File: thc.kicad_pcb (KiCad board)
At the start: 2 copper layers, 132 x 100 mm, 53 parts, among them CON1 BARREL_JACK, IC1 4N25, J1 DB9, J2 DB25, U1 LM358N, U2 ARDUINO_MINI_PRO, U3 CNY74-4, U4 7805, U5 ISOL_PWR, U6 LM324N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

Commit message: Finalized design, produced PCB, started testing it
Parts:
- added Q1: BC547, TO92, F.Cu at (73.9, 39.8)
- added R22: 10K, R3-LARGE_PADS, F.Cu at (70.7, 49.0)
- added R23: 1K, R3-LARGE_PADS, F.Cu at (78.0, 33.5)
- R21: value 100R -> 1K
- U6: value LM324N -> 74HC04
- moved R15 9.25 mm to (136.5, 66.7), turned to 180 degrees
- moved D4 8.25 mm to (78.0, 44.2)
- moved R13 7.96 mm to (143.5, 43.8)
- moved C2 7.74 mm to (134.6, 46.2)
- moved J2 6.41 mm to (140.2, 95.8)
- moved R12 3.24 mm to (138.4, 43.8)
- moved U6 2.62 mm to (141.0, 54.6)
- moved R14 1.42 mm to (132.1, 62.9), turned to 180 degrees
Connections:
- D4 pad 2: N-0000010 -> N-000006
- J2 pad 18: (no net) -> GNDA
- J2 pad 19: (no net) -> GNDA
- J2 pad 20: (no net) -> GNDA
- J2 pad 21: (no net) -> GNDA
- J2 pad 22: (no net) -> GNDA
- J2 pad 23: (no net) -> GNDA
- J2 pad 24: (no net) -> GNDA
- J2 pad 25: (no net) -> GNDA
- R12 pad 1: N-0000039 -> N-0000048
- R13 pad 1: N-0000040 (its old number) -> N-0000049
- R14 pad 1: N-0000041 -> N-0000051
- R15 pad 1: N-0000038 (its old number) -> N-0000050
- R16 pad 1: I_THC_INP3 -> I_THC_INP4
- R17 pad 1: I_THC_INP4 -> I_THC_INP3
- R21 pad 2: N-0000010 -> N-0000023
- U2 pad 10: I_THC_INP3 -> I_THC_INP4
- U2 pad 6: N-0000010 -> N-000006
- U2 pad 9: I_THC_INP4 -> I_THC_INP3
- U6 pad 1: N-0000041 -> /Isolation/U_THC_INP4
- U6 pad 10: /Isolation/U_THC_INP2 -> N-0000049
- U6 pad 11: GNDA -> /Isolation/U_THC_INP2
- U6 pad 12: /Isolation/U_THC_INP1 -> N-0000048
- U6 pad 13: N-0000039 -> /Isolation/U_THC_INP1
- U6 pad 14: N-0000039 -> +5VA
- U6 pad 2: N-0000041 -> N-0000051
- U6 pad 4: +5VA -> N-0000050
- U6 pad 5: /Isolation/U_THC_INP4 -> (no net)
- U6 pad 6: N-0000038 (its old number) -> (no net)
- U6 pad 7: N-0000038 (its old number) -> GNDA
- U6 pad 8: N-0000040 (its old number) -> (no net)
- U6 pad 9: N-0000040 (its old number) -> (no net)
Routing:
- net GNDA: track 228.7 -> 320.3 mm
- net +5V: track 146.2 -> 200.5 mm, vias 2 -> 3
- net /Isolation/U_THC_INP3: track 61.7 -> 26.5 mm
- net N-0000010: track 32.9 -> 0.00 mm
- net N-000006: track 0.00 -> 28.4 mm
- net /Isolation/U_THC_INP4: track 56.0 -> 29.6 mm
- net /Isolation/U_THC_OUT1: track 128.6 -> 107.7 mm, vias 0 -> 2
- net +5VA: track 144.8 -> 126.3 mm
- net GND: track 423.1 -> 440.4 mm
- net N-0000046: track 31.0 -> 17.8 mm
- net /Isolation/U_THC_OUT5: track 81.5 -> 68.4 mm
- net /Isolation/U_THC_OUT4: track 79.6 -> 67.4 mm
- net N-0000023: track 0.00 -> 11.1 mm
- net I_THC_OUT4: track 66.6 -> 77.3 mm
- net /Isolation/U_THC_INP2: track 54.1 -> 44.8 mm
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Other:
- board size 132 x 100 mm -> 130 x 100 mm
- board text added: "RV2014"
- board text added: "THC"

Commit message: Done some more tests
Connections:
- U2 pad 21: (no net) -> /AMP_SIG

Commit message: Fixes completely wrong schematics and PCB layout
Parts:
- removed D10, D11, D12, D13: ZENER, D3
- moved R18 1.91 mm to (109.3, 50.8), turned to 180 degrees
- moved R17 1.22 mm to (109.4, 53.4), turned to 180 degrees
- moved R16 0.20 mm to (109.4, 61.0)
- turned R19 to 180 degrees
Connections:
- R16 pad 1: I_THC_INP4 -> GND
- R16 pad 2: N-0000063 -> I_THC_INP4
- R17 pad 2: N-0000066 (its old number) -> GND
- R18 pad 2: N-0000065 (its old number) -> GND
- R19 pad 2: N-0000064 -> GND
- U7 pad 10: GND -> +5V
- U7 pad 11: GND -> +5V
- U7 pad 12: N-0000065 (its old number) -> I_THC_INP2
- U7 pad 13: N-0000066 (its old number) -> I_THC_INP3
- U7 pad 14: GND -> +5V
- U7 pad 15: GND -> +5V
- U7 pad 16: N-0000063 -> I_THC_INP4
- U7 pad 9: N-0000064 -> I_THC_INP1
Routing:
- net +5V: track 200.5 -> 249.2 mm
- net I_THC_INP4: track 62.6 -> 84.1 mm
- net I_THC_INP2: track 55.1 -> 75.8 mm
- net GND: track 440.4 -> 420.6 mm, vias 0 -> 2
- net I_THC_INP1: track 51.5 -> 70.6 mm
- net I_THC_INP3: track 59.1 -> 77.7 mm
- net N-0000064: track 11.8 -> 0.00 mm
- net N-0000063: track 11.8 -> 0.00 mm
- net N-0000065 (its old number): track 6.50 -> 0.00 mm
- net N-0000066 (its old number): track 6.24 -> 0.00 mm

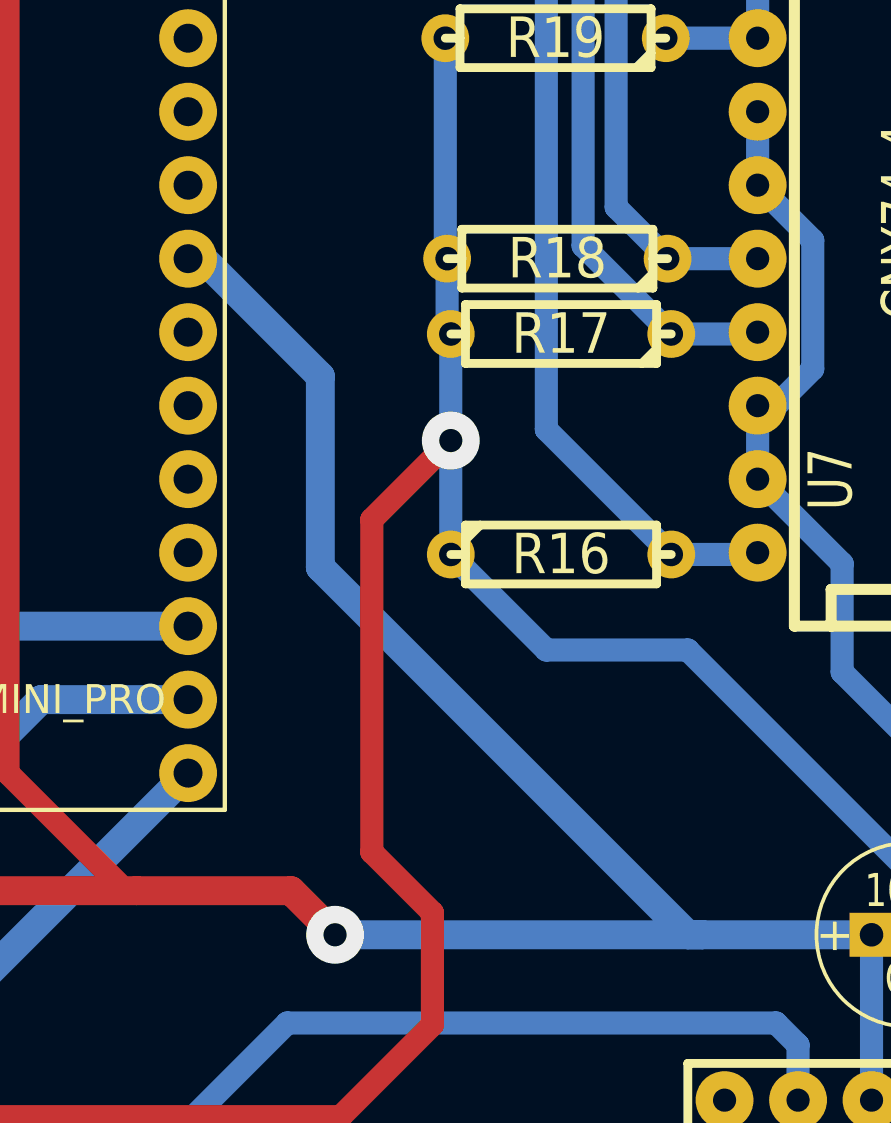
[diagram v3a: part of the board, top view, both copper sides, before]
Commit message: Fixed wrong power pin being used in Atmega
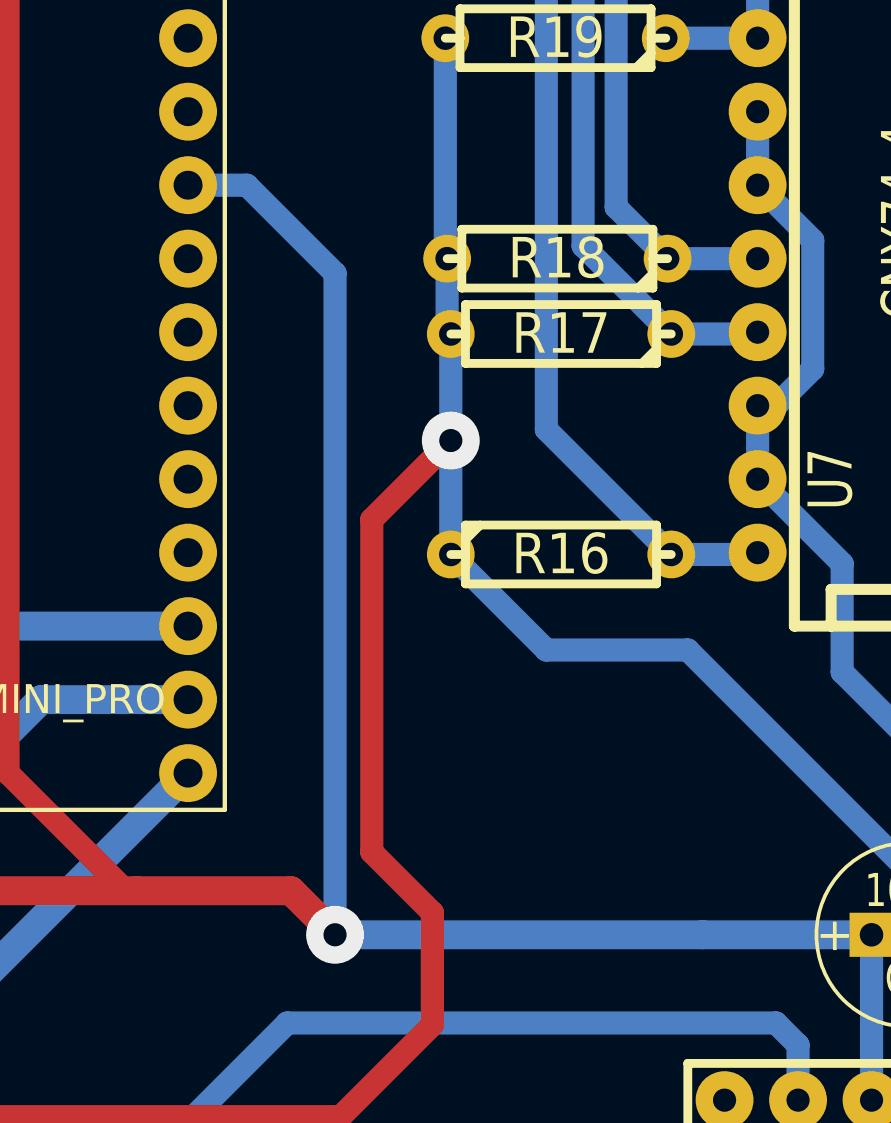
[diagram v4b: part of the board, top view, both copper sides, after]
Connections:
- U2 pad 24: +5V -> (no net)
- U2 pad 25: (no net) -> +5V
- U2 pad 27: (no net) -> GND
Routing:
- net +5V: track 249.2 -> 247.0 mm

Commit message: Finished sensor board, started layout of controller board
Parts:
- removed J1: DB9, DB9FC
- added C10: 0.1uF, C1, F.Cu at (-15.2, -29.2)
- added C11: 0.1uF, C1, F.Cu at (-31.9, -16.5)
- added C12: 10uF, C1V7, F.Cu at (-19.7, -18.4)
- added C8: 0.1uF, C1, F.Cu at (-33.0, -20.3)
- added C9: 10uF, C1V7, F.Cu at (-46.4, -14.0)
- added D10: 5v1 ZENER, D3, F.Cu at (-49.5, -20.3)
- added J3: DB9, DB9FC, F.Cu at (38.1, 48.3)
- added PH1: IL300, DIP-8__300_ELL, F.Cu at (55.2, 18.4)
- added R24: 400R, R3-LARGE_PADS, F.Cu at (-50.8, -2.54)
- added R25: 230R, R3-LARGE_PADS, F.Cu at (-40.0, -24.8)
- added R26: 400R, R3-LARGE_PADS, F.Cu at (-48.3, -27.9)
- added R27: 1K, R3-LARGE_PADS, F.Cu at (-31.8, -29.2)
- added R28: 1K, R3-LARGE_PADS, F.Cu at (-20.3, -12.1)
- added R29: 400R, R3-LARGE_PADS, F.Cu at (-34.9, -11.4)
- added U8: ISOL_PWR, SIL-4, F.Cu at (-23.5, -24.8)
- C1: value 1uF -> 0.1uF
- D1, D3, D4, D5, D6, D7, D8, D9: value ZENER -> 5v1 ZENER
- D2: value DIODE -> 1N4007
- R1, R16, R17, R18, R19, R2, R23, R4, R5, R6: value 1K -> 10K
- R21: value 1K -> 3K3
- R22: value 10K -> 75K
- R3: value 1K -> 100R
- U1: value LM358N -> LM358
- moved D6 14.6 mm to (90.2, 89.5)
- moved IC1 14.6 mm to (98.4, 90.8)
- moved R1 14.6 mm to (109.9, 119.4)
- moved R11 14.6 mm to (87.0, 89.5)
- moved R2 14.6 mm to (109.9, 111.8)
- moved R4 14.6 mm to (109.9, 109.2)
- moved R5 14.6 mm to (109.9, 101.6)
- moved R6 14.6 mm to (106.0, 89.5)
- moved U3 14.6 mm to (98.4, 110.5)
- moved D5 14.6 mm to (83.8, 97.2)
- moved D7 14.6 mm to (83.8, 103.5)
- moved D8 14.6 mm to (83.8, 109.9)
- moved D9 14.6 mm to (83.8, 116.8)
- moved R10 14.6 mm to (83.8, 100.3)
- moved R7 14.6 mm to (83.8, 120.0)
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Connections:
- C1 pad 1: +12V -> +12C
- C1 pad 2: GND -> VSS
- D1 pad 2: /AMP_SIG -> +5V
- D4 pad 2: N-000006 -> N-0000015
- Q1 pad 1: N-000006 -> +5V
- Q1 pad 2: N-0000023 -> N-0000081
- Q1 pad 3: GND -> N-0000074
- R20 pad 1: /TORCH_ON -> I_TORCH_ON
- R21 pad 1: /ARC_OK -> N-0000081
- R21 pad 2: N-0000023 -> I_TORCH_ON
- R22 pad 1: GND -> N-0000082
- R22 pad 2: N-0000023 -> VSS
- R23 pad 1: N-000006 -> GND
- R23 pad 2: +5V -> N-0000081
- R3 pad 1: N-0000022 -> I_ARC_OK
- R3 pad 2: /AMP_SIG -> N-0000015
- U1 pad 1: N-0000022 -> N-0000085
- U1 pad 2: N-0000022 -> N-0000082
- U1 pad 3: /FILT_SIG -> /Plasma source/ANALOG_IN
- U1 pad 4: GND -> VSS
- U1 pad 5: (no net) -> N-0000084
- U1 pad 6: (no net) -> I_ANALOG_IN
- U1 pad 7: (no net) -> I_ANALOG_IN
- U1 pad 8: +12V -> +12C
- U2 pad 21: /AMP_SIG -> I_ANALOG_IN
- U2 pad 6: N-000006 -> N-0000015
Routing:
- net GND: track 420.6 -> 179.4 mm, vias 2 -> 0
- net +5V: track 247.0 -> 106.6 mm, vias 3 -> 0
- net +12V: track 151.7 -> 32.7 mm, vias 2 -> 0
- net /Isolation/U_THC_OUT1: track 107.7 -> 3.81 mm, vias 2 -> 0
- net I_THC_OUT1: track 83.8 -> 0.00 mm
- net GNDA: track 320.3 -> 237.7 mm
- net I_THC_OUT4: track 77.3 -> 0.00 mm
- net I_THC_OUT5: track 73.7 -> 0.00 mm
- net /Isolation/U_THC_OUT5: track 68.4 -> 3.81 mm
- net I_THC_OUT3: track 63.6 -> 0.00 mm
- net /Isolation/U_THC_OUT4: track 67.4 -> 3.81 mm
- net /Isolation/U_THC_OUT2: track 61.6 -> 3.81 mm
- net /Isolation/U_THC_OUT3: track 61.4 -> 3.81 mm
- net I_THC_OUT2: track 46.3 -> 0.00 mm
- net /ARC_OK: track 42.6 -> 0.00 mm
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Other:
- board size 130 x 100 mm -> 318 x 243.5 mm
- board text removed: "RV2014"
- board text removed: "THC"

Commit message: Finalized new PCB
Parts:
- removed D1: 5v1 ZENER, D3
- added 1PIN: P***, 1pin, F.Cu at (38.1, 101.6)
- added 1PIN: P***, 1pin, F.Cu at (80.0, 31.8)
- added 1PIN: P***, 1pin, F.Cu at (135.9, 33.0)
- added 1PIN: P***, 1pin, F.Cu at (135.9, 121.9)
- added IC2: 4N25, DIP-6__300_ELL, F.Cu at (62.2, 48.5)
- added IC3: 4N25, DIP-6__300_ELL, F.Cu at (61.0, 35.3)
- added U9: LM358, DIP-8__300_ELL, F.Cu at (71.1, 72.6)
- R29: value 400R -> 38K
- moved D10 163.3 mm to (100.3, 44.5), turned to 270 degrees
- moved C9 155.3 mm to (64.1, 95.1), turned to 90 degrees
- moved C8 145.0 mm to (71.4, 80.3)
- moved C10 144.8 mm to (59.1, 95.1), turned to 90 degrees
- moved U8 141.3 mm to (55.2, 92.6), turned to 90 degrees
- moved R26 140.7 mm to (45.7, 76.7)
- moved C11 135.2 mm to (51.4, 90.0), turned to 90 degrees
- moved R29 131.1 mm to (71.4, 65.3), turned to 180 degrees
- moved C12 127.0 mm to (46.4, 90.0), turned to 90 degrees
- moved R27 125.6 mm to (69.8, 44.7), turned to 90 degrees
- moved R25 121.8 mm to (69.1, 29.5)
- moved R24 112.5 mm to (50.8, 45.7), turned to 180 degrees
- moved R28 85.0 mm to (50.3, 35.3), turned to 180 degrees
- moved PH1 59.6 mm to (56.5, 78.0), turned to 270 degrees
- moved C1 43.8 mm to (33.0, 78.1)
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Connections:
- C10 pad 1: +12V -> N-0000084
- C12 pad 1: (no net) -> +12C
- C8 pad 1: +5V -> +12V
- C9 pad 1: +12V -> N-0000084
- PH1 pad 5: N-0000084 -> N-0000085
- R29 pad 2: N-0000084 -> N-0000085
- U1 pad 5: N-0000084 -> (no net)
- U1 pad 6: I_ANALOG_IN -> (no net)
- U1 pad 7: I_ANALOG_IN -> (no net)
- U8 pad 1: +12V -> N-0000084
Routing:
- net +5V: track 106.6 -> 270.4 mm, vias 0 -> 7
- net VSS: track 0.00 -> 156.7 mm, vias 0 -> 2
- net GND: track 179.4 -> 324.8 mm, vias 0 -> 1
- net +12C: track 0.00 -> 116.7 mm
- net /Isolation/U_THC_OUT1: track 3.81 -> 71.0 mm, vias 0 -> 2
- net I_THC_OUT1: track 0.00 -> 56.0 mm
- net /Isolation/U_THC_OUT5: track 3.81 -> 56.3 mm
- net /Isolation/U_THC_OUT4: track 3.81 -> 53.7 mm
- net I_THC_OUT5: track 0.00 -> 46.0 mm
- net I_THC_OUT4: track 0.00 -> 44.1 mm
- net /Isolation/U_THC_OUT3: track 3.81 -> 47.5 mm
- net I_ANALOG_IN: track 0.00 -> 42.4 mm, vias 0 -> 2
- net +12V: track 32.7 -> 72.4 mm
- net GNDA: track 237.7 -> 199.6 mm
- net /Isolation/U_THC_OUT2: track 3.81 -> 40.7 mm
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- added copper zone on B.Cu, net GND
- added copper zone on B.Cu, net GNDA
- added copper zone on B.Cu, net VSS
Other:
- board size 318 x 243.5 mm -> 320.1 x 243.5 mm
- board text added: "RV2014 THC v2"

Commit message: Changed sensor board to contain less resistors
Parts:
- U8: footprint SIL-4 -> MCE_DIP
- moved C12 8.11 mm to (38.6, 87.6), turned to 270 degrees
- moved U8 5.78 mm to (49.8, 94.5), turned to 0 degrees
- moved C11 5.31 mm to (49.5, 85.1), turned to 0 degrees
- moved C1 1.17 mm to (33.3, 77.0)
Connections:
- C10 pad 1: N-0000084 (its old number) -> GND
- C10 pad 2: GND -> +12V
- C11 pad 1: +12C -> VSS
- C11 pad 2: VSS -> +12C
- C12 pad 1: +12C -> VSS
- C12 pad 2: VSS -> +12C
- C9 pad 1: N-0000084 (its old number) -> GND
- C9 pad 2: GND -> +12V
- U8 pad 1: N-0000084 (its old number) -> GND
- U8 pad 2: GND -> +12V
- U8 pad 3: +12C -> VSS
- U8 pad 4: VSS -> +12C
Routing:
- net +12V: track 72.4 -> 106.5 mm
- net +12C: track 116.7 -> 142.4 mm
- net VSS: track 156.7 -> 168.5 mm
- net GND: track 324.8 -> 314.0 mm
- net N-0000084 (its old number): track 8.89 -> 0.00 mm
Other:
- board size 320.1 x 243.5 mm -> 123.8 x 99.7 mm

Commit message: Added Zener diodes on IO from plasma source
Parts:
- added D1: 5v1 ZENER, D3, F.Cu at (48.3, 52.7)
- added D11: 12v1 ZENER, D3, F.Cu at (41.9, 40.0)
- added D12: 12v1 ZENER, D3, F.Cu at (47.0, 30.5)
- R22: value 75K -> 47k
- R29: value 38K -> 47k
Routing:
- net VSS: track 168.5 -> 156.2 mm
- net /Plasma source/ARC_OK: track 14.1 -> 19.3 mm
- net /Plasma source/TORCH_ON: track 33.5 -> 35.4 mm
- net /Plasma source/ANALOG_IN: track 30.8 -> 32.1 mm
